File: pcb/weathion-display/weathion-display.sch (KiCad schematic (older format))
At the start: 4 parts

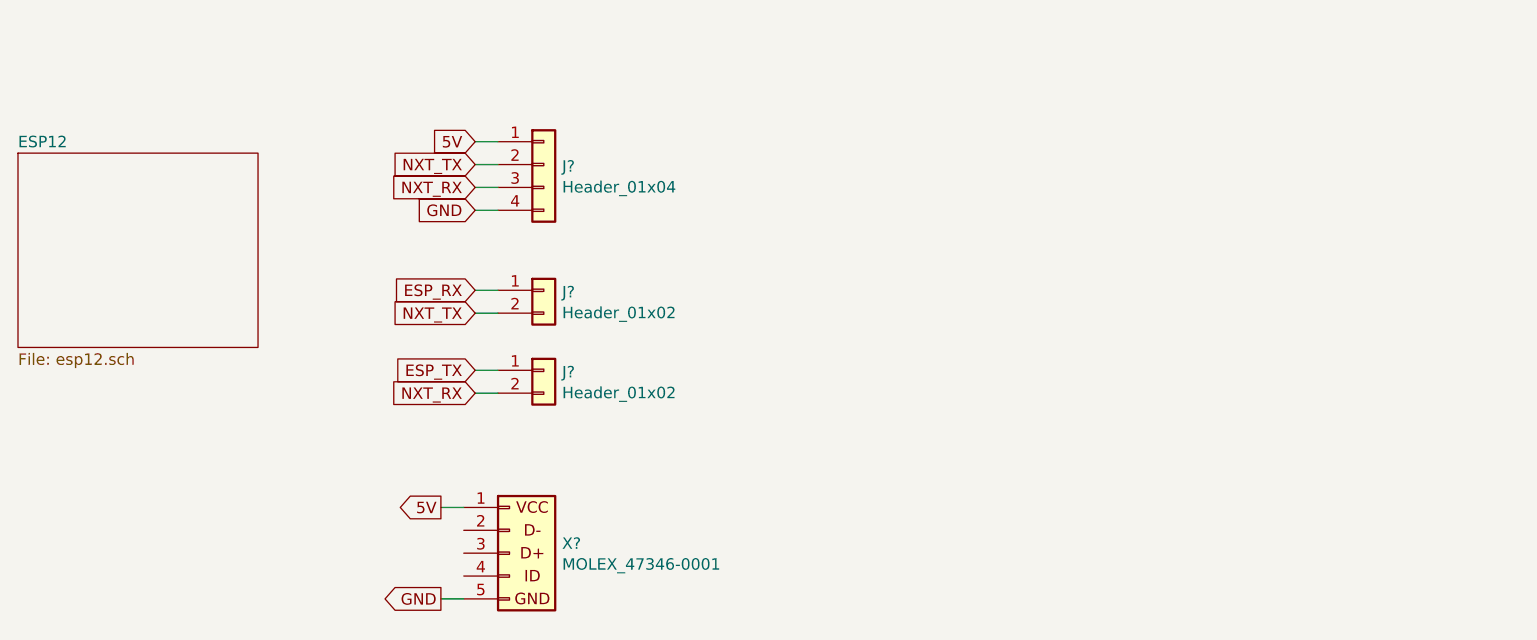
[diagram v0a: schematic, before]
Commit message: full schematic done
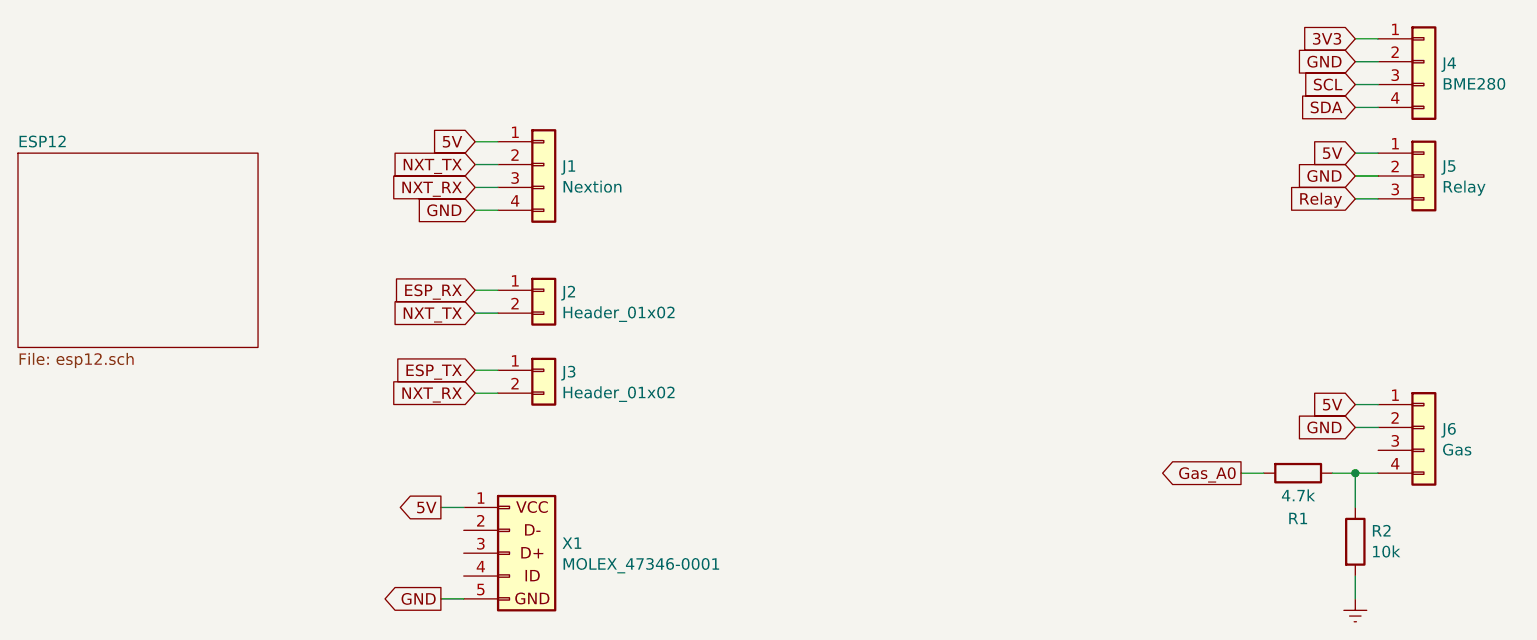
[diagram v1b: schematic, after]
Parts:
- added J4: BME280, Connector_Header:PinHeader_1x04_P2.54mm_Vertical, symbol Connector_Header:Header_01x04
- added J5: Relay, Connector_Header:PinHeader_1x03_P2.54mm_Vertical, symbol Connector_Header:Header_01x03
- added J6: Gas, Connector_Header:PinHeader_1x04_P2.54mm_Vertical, symbol Connector_Header:Header_01x04
- added R1: 4.7k, Resistors:R_0603, symbol Resistor_0603:R
- added R2: 10k, Resistors:R_0603, symbol Resistor_0603:R
- J1: renamed from J?; value Header_01x04 -> Nextion; footprint (none) -> Connector_Header:PinHeader_1x04_P2.54mm_Vertical
- J2, J3: renamed from J?; footprint (none) -> Connector_Header:PinHeader_1x02_P2.54mm_Vertical
- gave numbers to parts that had none: 1
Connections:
- net 5V: now also J5.1 (Pin_1), J6.1 (Pin_1)
- net GND: now also J4.2 (Pin_2), J5.2 (Pin_2), J6.2 (Pin_2)
- new net: J6.4 (Pin_4), R1.1, R2.1
- new net 3V3: J4.1 (Pin_1)
- new net Earth: R2.2
- new net Gas_A0: R1.2
- new net Relay: J5.3 (Pin_3)
- new net SCL: J4.3 (Pin_3)
- new net SDA: J4.4 (Pin_4)
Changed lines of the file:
@@
 $EndDescr
 $Comp
-L Connector_Header:Header_01x04 J?
+L Connector_Header:Header_01x04 J1
 U 1 1 5E5A025D
 P 4100 1750
-F 0 "J?" H 4180 1792 50  0000 L CNN
-F 1 "Header_01x04" H 4180 1701 50  0000 L CNN
-F 2 "" H 4100 1700 50  0001 C CNN
+F 0 "J1" H 4180 1792 50  0000 L CNN
+F 1 "Nextion" H 4180 1701 50  0000 L CNN
+F 2 "Connector_Header:PinHeader_1x04_P2.54mm_Vertical" H 4100 1700 50  0001 C CNN
 F 3 "" H 4100 1700 50  0001 C CNN
 	1    4100 1750
@@
 	3800 1900 3900 1900
 $Comp
-L Connector_Header:Header_01x02 J?
+L Connector_Header:Header_01x02 J2
 U 1 1 5E5A3835
 P 4100 2300
-F 0 "J?" H 4180 2342 50  0000 L CNN
+F 0 "J2" H 4180 2342 50  0000 L CNN
 F 1 "Header_01x02" H 4180 2251 50  0000 L CNN
-F 2 "" H 4100 2150 50  0001 C CNN
+F 2 "Connector_Header:PinHeader_1x02_P2.54mm_Vertical" H 4100 2150 50  0001 C CNN
 F 3 "" H 4100 2150 50  0001 C CNN
 	1    4100 2300
@@
 $EndComp
 $Comp
-L Connector_Header:Header_01x02 J?
+L Connector_Header:Header_01x02 J3
 U 1 1 5E5A3EBB
 P 4100 2650
-F 0 "J?" H 4180 2692 50  0000 L CNN
+F 0 "J3" H 4180 2692 50  0000 L CNN
 F 1 "Header_01x02" H 4180 2601 50  0000 L CNN
-F 2 "" H 4100 2500 50  0001 C CNN
+F 2 "Connector_Header:PinHeader_1x02_P2.54mm_Vertical" H 4100 2500 50  0001 C CNN
 F 3 "" H 4100 2500 50  0001 C CNN
 	1    4100 2650
@@
 $EndSheet
 $Comp
-L Connector_USB:MOLEX_47346-0001 X?
+L Connector_USB:MOLEX_47346-0001 X1
 U 1 1 5E5C62FE
 P 3950 3400
-F 0 "X?" H 4180 3442 50  0000 L CNN
+F 0 "X1" H 4180 3442 50  0000 L CNN
 F 1 "MOLEX_47346-0001" H 4180 3351 50  0000 L CNN
 F 2 "Connector_USB:USB_Micro-B_Molex_47346-0001" H 4050 2900 50  0001 C CIN
@@
 Wire Wire Line
 	3750 3600 3650 3600
+$Comp
+L Connector_Header:Header_01x03 J5
+U 1 1 5E558A16
+P 7950 1800
+F 0 "J5" H 8030 1892 50  0000 L CNN
+F 1 "Relay" H 8030 1801 50  0000 L CNN
+F 2 "Connector_Header:PinHeader_1x03_P2.54mm_Vertical" H 7950 1750 50  0001 C CNN
+F 3 "" H 7950 1750 50  0001 C CNN
+	1    7950 1800
+	1    0    0    -1
+$EndComp
+$Comp
+L Connector_Header:Header_01x04 J6
+U 1 1 5E558DDF
+P 7950 2900
+F 0 "J6" H 8030 2942 50  0000 L CNN
+F 1 "Gas" H 8030 2851 50  0000 L CNN
+F 2 "Connector_Header:PinHeader_1x04_P2.54mm_Vertical" H 7950 2850 50  0001 C CNN
+F 3 "" H 7950 2850 50  0001 C CNN
+	1    7950 2900
+	1    0    0    -1
+$EndComp
+Text GLabel 7650 2750 0    50   Input ~ 0
+5V
+Text GLabel 7650 2850 0    50   Input ~ 0
+GND
+Text GLabel 7150 3050 0    50   Output ~ 0
+Gas_A0
+$Comp
+L Resistor_0603:R R1
+U 1 1 5E55D7B2
+P 7400 3050
+F 0 "R1" V 7600 3050 50  0000 C CNN
+F 1 "4.7k" V 7500 3050 50  0000 C CNN
+F 2 "Resistors:R_0603" V 7330 3050 50  0001 C CNN
+F 3 "~" H 7400 3050 50  0001 C CNN
+	1    7400 3050
+	0    1    1    0
+$EndComp
+$Comp
+L Resistor_0603:R R2
+U 1 1 5E55F930
+P 7650 3350
+F 0 "R2" H 7720 3396 50  0000 L CNN
+F 1 "10k" H 7720 3305 50  0000 L CNN
+F 2 "Resistors:R_0603" V 7580 3350 50  0001 C CNN
+F 3 "~" H 7650 3350 50  0001 C CNN
+	1    7650 3350
+	1    0    0    -1
+$EndComp
+Wire Wire Line
+	7750 3050 7650 3050
+Wire Wire Line
+	7250 3050 7150 3050
+Wire Wire Line
+	7650 3200 7650 3050
+Connection ~ 7650 3050
+Wire Wire Line
+	7650 3050 7550 3050
+$Comp
+L Power:GND #PWR0101
+U 1 1 5E562CDA
+P 7650 3600
+F 0 "#PWR0101" H 7650 3350 50  0001 C CNN
+F 1 "GND" H 7650 3450 50  0001 C CNN
+F 2 "" H 7650 3600 50  0001 C CNN
+F 3 "~" H 7650 3600 50  0001 C CNN
+	1    7650 3600
+	1    0    0    -1
+$EndComp
+Wire Wire Line
+	7650 3600 7650 3500
+Wire Wire Line
+	7650 2850 7750 2850
+Wire Wire Line
+	7650 2750 7750 2750
+Text GLabel 7650 1650 0    50   Input ~ 0
+5V
+Text GLabel 7650 1750 0    50   Input ~ 0
+GND
+Text GLabel 7650 1850 0    50   Input ~ 0
+Relay
+Wire Wire Line
+	7650 1650 7750 1650
+Wire Wire Line
+	7650 1750 7750 1750
+Wire Wire Line
+	7650 1850 7750 1850
+$Comp
+L Connector_Header:Header_01x04 J4
+U 1 1 5E572B0E
+P 7950 1300
+F 0 "J4" H 8030 1342 50  0000 L CNN
+F 1 "BME280" H 8030 1251 50  0000 L CNN
+F 2 "Connector_Header:PinHeader_1x04_P2.54mm_Vertical" H 7950 1250 50  0001 C CNN
+F 3 "" H 7950 1250 50  0001 C CNN
+	1    7950 1300
+	1    0    0    -1
+$EndComp
+Text GLabel 7650 1150 0    50   Input ~ 0
+3V3
+Text GLabel 7650 1250 0    50   Input ~ 0
+GND
+Text GLabel 7650 1350 0    50   Input ~ 0
+SCL
+Text GLabel 7650 1450 0    50   Input ~ 0
+SDA
+Wire Wire Line
+	7650 1150 7750 1150
+Wire Wire Line
+	7650 1250 7750 1250
+Wire Wire Line
+	7650 1350 7750 1350
+Wire Wire Line
+	7650 1450 7750 1450
 $EndSCHEMATC
